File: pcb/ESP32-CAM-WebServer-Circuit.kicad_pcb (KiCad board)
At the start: 2 copper layers, 30.5 x 48.3 mm, 12 parts, among them IC1 ESP32-CAM, J1 Conn_01x02, Q1 2N7002, Q2 IRLML0030, SW1 SW_SPDT, U1 TP4056-Module, U2 XC6503D331MR-G

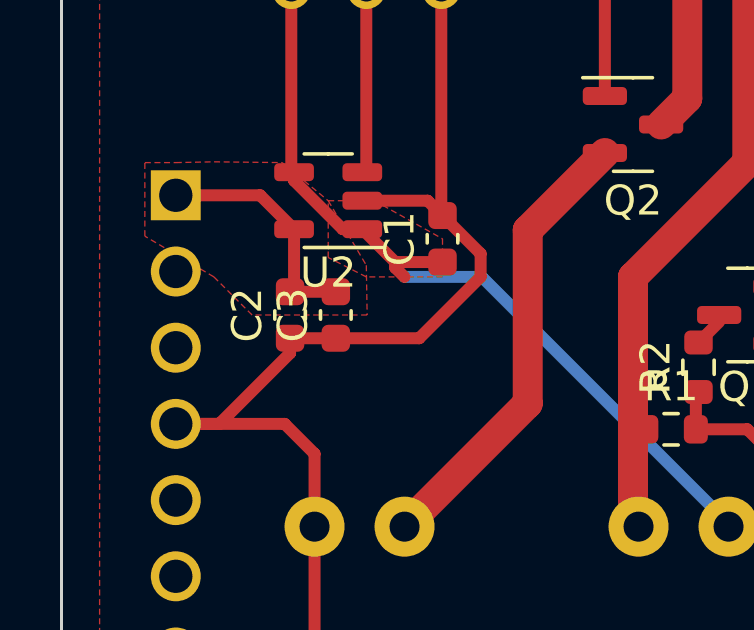
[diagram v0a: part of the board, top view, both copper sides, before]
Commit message: Revert "change(pcb): move C3 outside C2 courtyard"
This reverts commit 39996186d04dd1fe4f6352967fedf0a05c03e2e3.
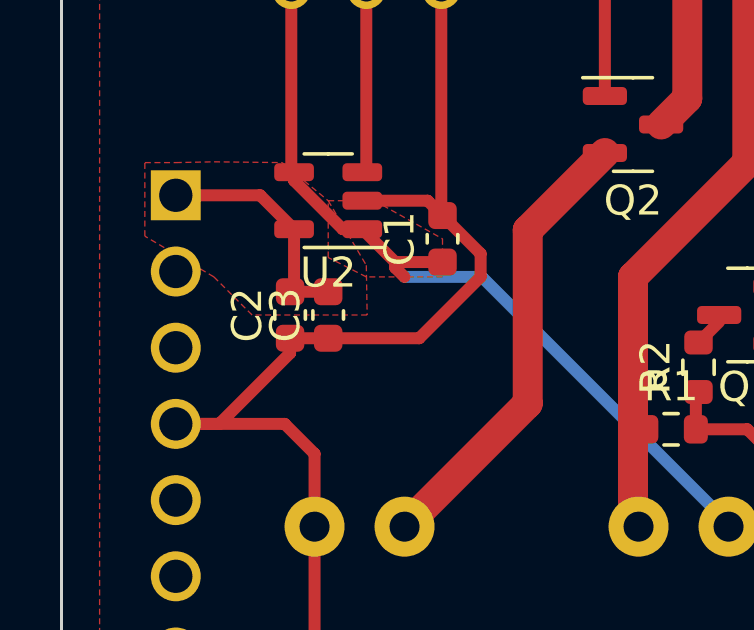
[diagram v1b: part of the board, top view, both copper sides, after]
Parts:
- moved C3 0.25 mm to (157.5, 62.2)
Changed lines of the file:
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@@
   )
   (footprint "Capacitor_SMD:C_0603_1608Metric" (layer "F.Cu")
-    (at 157.734 62.23 90)
+    (at 157.48 62.23 90)
     (descr "Capacitor SMD 0603 (1608 Metric), square (rectangular) end terminal, IPC_7351 nominal, (Body size source: IPC-SM-782 page 76, https://www.pcb-3d.com/wordpress/wp-content/uploads/ipc-sm-782a_amendment_1_and_2.pdf), generated with kicad-footprint-generator")
     (tags "capacitor")

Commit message: change(pcb): move C3 outside C2 courtyard
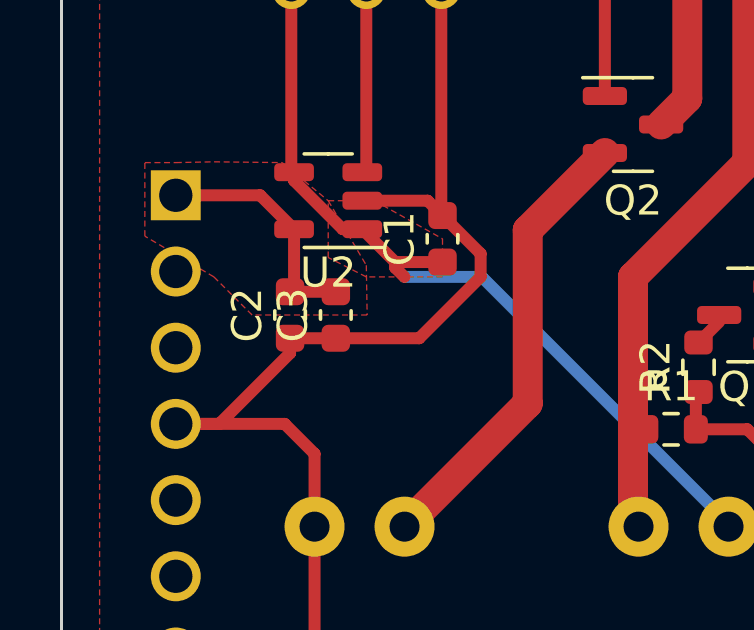
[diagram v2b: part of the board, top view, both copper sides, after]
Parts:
- moved C3 0.25 mm to (157.7, 62.2)
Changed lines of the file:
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@@
   )
   (footprint "Capacitor_SMD:C_0603_1608Metric" (layer "F.Cu")
-    (at 157.48 62.23 90)
+    (at 157.734 62.23 90)
     (descr "Capacitor SMD 0603 (1608 Metric), square (rectangular) end terminal, IPC_7351 nominal, (Body size source: IPC-SM-782 page 76, https://www.pcb-3d.com/wordpress/wp-content/uploads/ipc-sm-782a_amendment_1_and_2.pdf), generated with kicad-footprint-generator")
     (tags "capacitor")
